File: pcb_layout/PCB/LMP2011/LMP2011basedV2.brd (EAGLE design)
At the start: 53.4 x 25.4 mm, 44 parts, among them J1 10118194-0001LF, U1 TS5A23167DCUR, U2 LMP2011MF, U3 TS5A23166DCUR, U4 TS5A23166DCUR, U5 LTC6241CS8PBF, U6 LTC6240CS8PBF, X1 PN87520-S

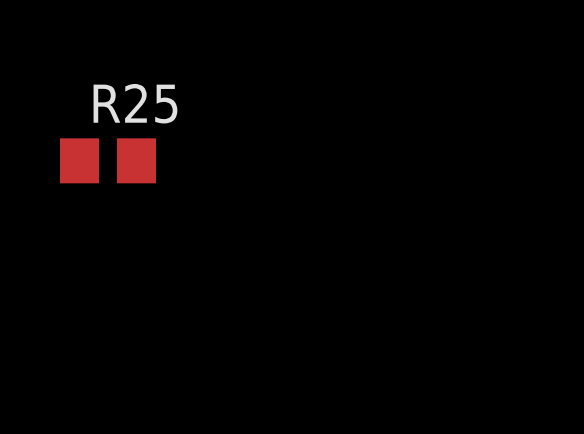
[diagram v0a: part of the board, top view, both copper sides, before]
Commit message: Added figures for LMP2011
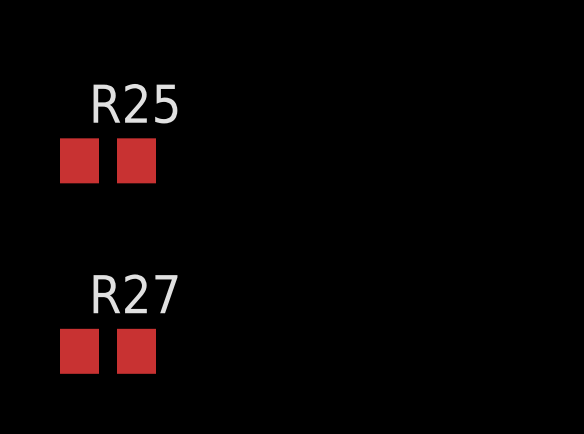
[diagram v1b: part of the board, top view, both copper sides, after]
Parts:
- added R27: 1k, resistor:R0805
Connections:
- net GND: now also R27.2
- net OUT_STAGE1: now also R27.1
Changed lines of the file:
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@@
 <element name="R24" library="resistor" library_urn="urn:adsk.eagle:library:348" package="R0805" package3d_urn="urn:adsk.eagle:package:26059/1" value="100k" x="-2.8575" y="-31.4325"/>
 <element name="R25" library="resistor" library_urn="urn:adsk.eagle:library:348" package="R0805" package3d_urn="urn:adsk.eagle:package:26059/1" value="100k" x="-2.8575" y="-37.7825"/>
+<element name="R27" library="resistor" library_urn="urn:adsk.eagle:library:348" package="R0805" package3d_urn="urn:adsk.eagle:package:26059/1" value="1k" x="-2.8575" y="-44.1325"/>
 </elements>
 <signals>
@@
 <contactref element="R23" pad="1"/>
 <contactref element="R22" pad="1"/>
+<contactref element="R27" pad="2"/>
 <wire x1="34.925" y1="23.8125" x2="37" y2="23.495" width="0" layer="19" extent="16-16"/>
 <wire x1="37" y1="21.2725" x2="37" y2="23.495" width="0" layer="19" extent="16-16"/>
@@
 <wire x1="-3.8075" y1="-31.4325" x2="-3.8075" y2="-25.0825" width="0" layer="19" extent="1-1"/>
 <wire x1="-3.8075" y1="-37.7825" x2="-3.8075" y2="-31.4325" width="0" layer="19" extent="1-1"/>
+<wire x1="-1.9075" y1="-44.1325" x2="-3.8075" y2="-37.7825" width="0" layer="19" extent="1-1"/>
 </signal>
 <signal name="N$2">
@@
 <wire x1="23.4975" y1="14.9225" x2="22.545" y2="14.9225" width="0.2032" layer="1"/>
 <wire x1="22.545" y1="14.9225" x2="21.5925" y2="15.875" width="0.2032" layer="1"/>
+<contactref element="R27" pad="1"/>
+<wire x1="13.2588" y1="13.6525" x2="-3.8075" y2="-44.1325" width="0" layer="19" extent="1-1"/>
 </signal>
 <signal name="N$12">
